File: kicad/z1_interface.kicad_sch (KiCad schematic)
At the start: 0 parts

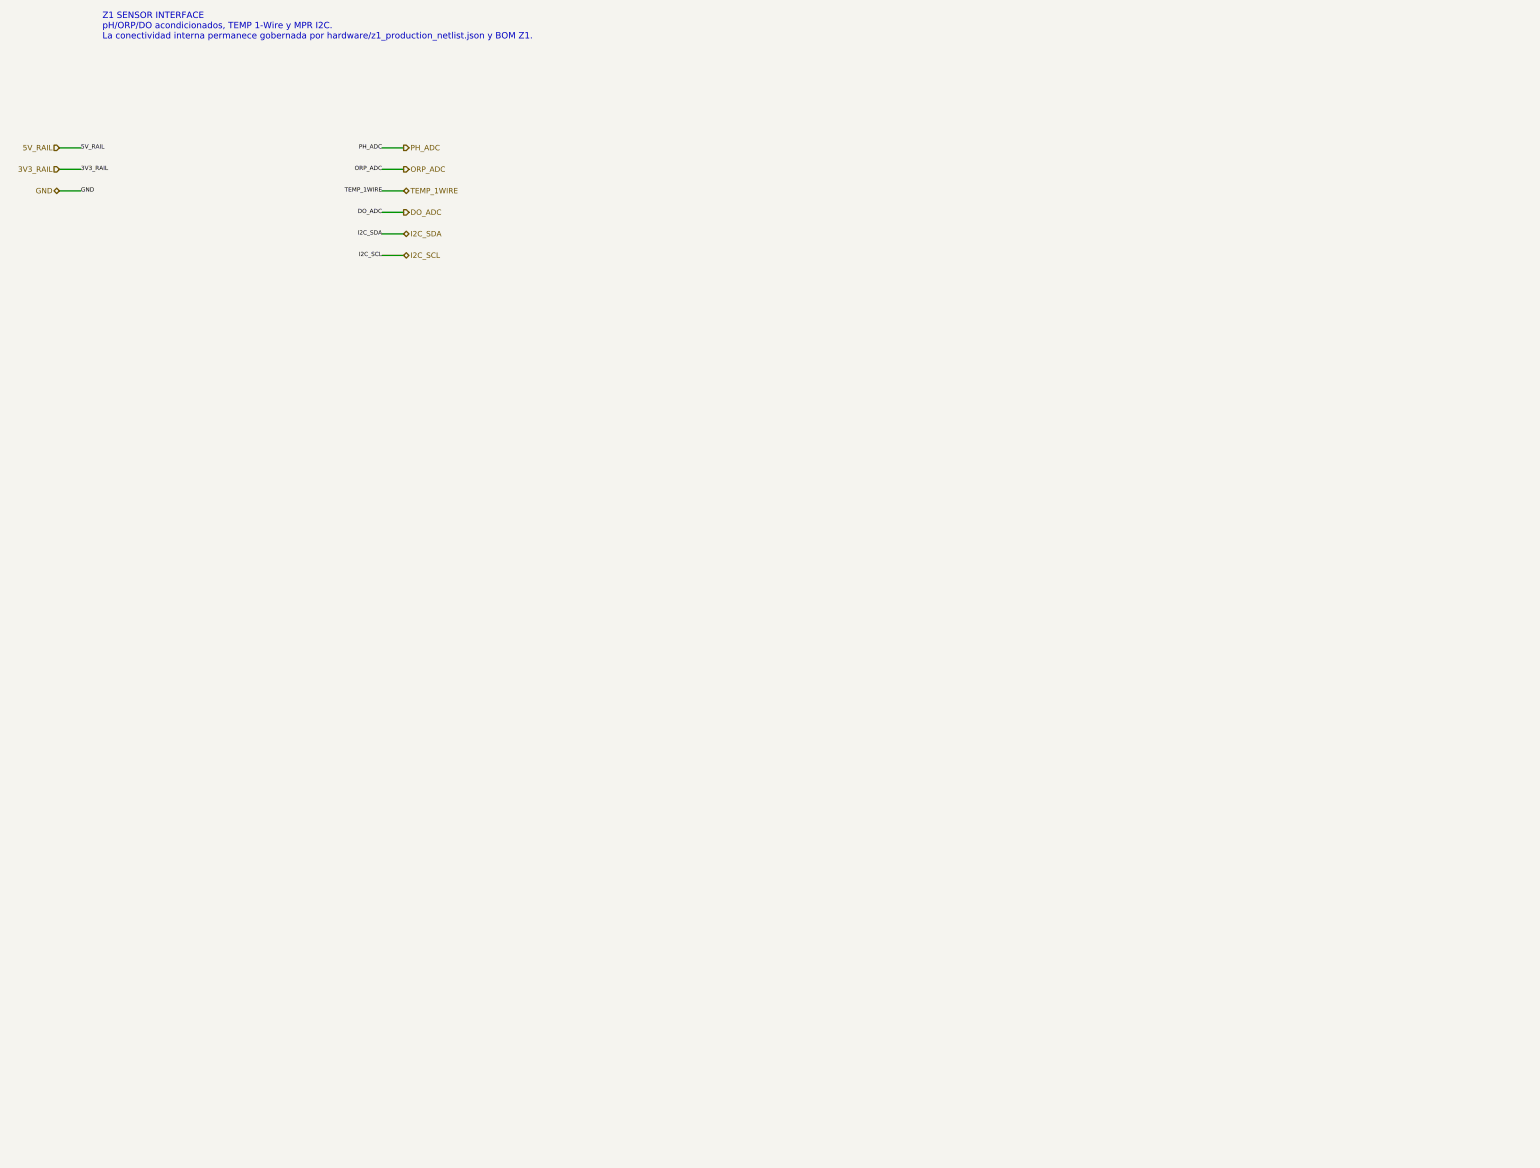
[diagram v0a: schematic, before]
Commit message: eda: materializar hierarchy de producción y cerrar ERC en cero (#15)
Materializa Z0–Z4 de forma determinista desde JSON/BOM, registra NFB_GEN, cierra seis links físicos verificados, elimina la deuda ERC de PR #14 y congela ERC=0/0 antes de placement. Mantiene placement, routing y geometría PCB fuera de alcance.
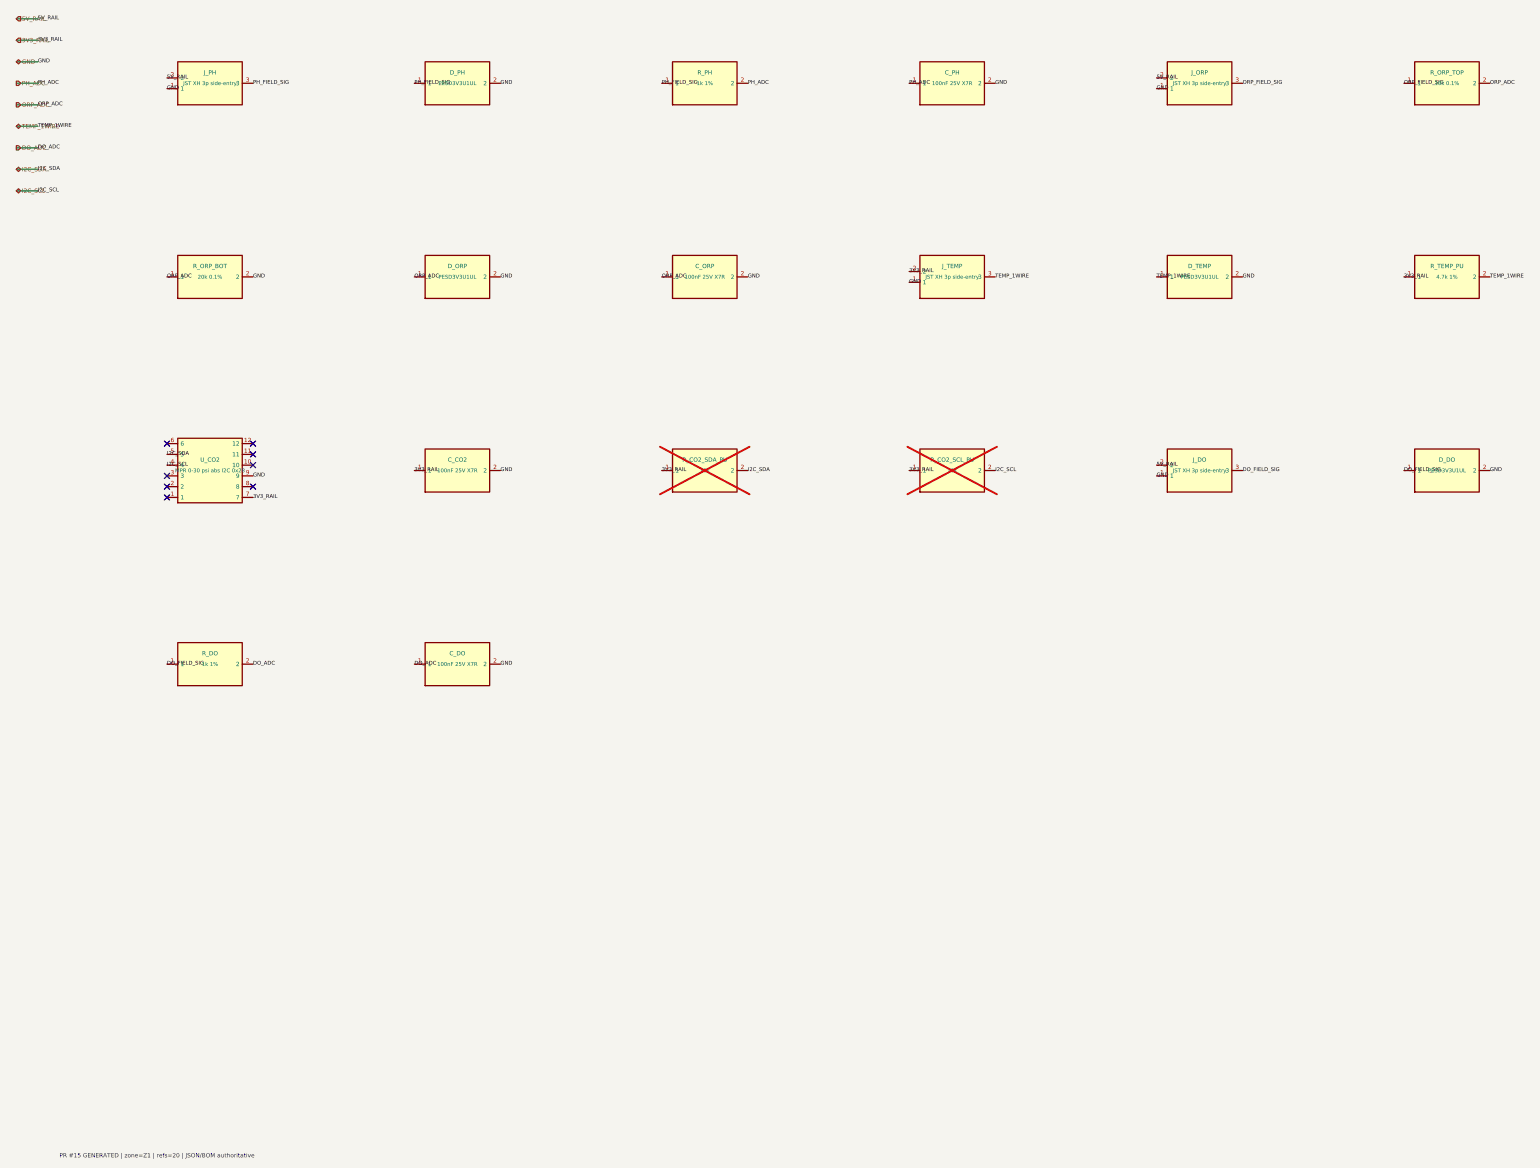
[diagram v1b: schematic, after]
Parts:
- added C_CO2: 100nF 25V X7R, Capacitor_SMD:C_0402_1005Metric, symbol NFB_GEN:SYM_C_CO2
- added C_DO: 100nF 25V X7R, Capacitor_SMD:C_0402_1005Metric, symbol NFB_GEN:SYM_C_DO
- added C_ORP: 100nF 25V X7R, Capacitor_SMD:C_0402_1005Metric, symbol NFB_GEN:SYM_C_ORP
- added C_PH: 100nF 25V X7R, Capacitor_SMD:C_0402_1005Metric, symbol NFB_GEN:SYM_C_PH
- added D_DO: PESD3V3U1UL, Diode_SMD:D_SOD-882, symbol NFB_GEN:SYM_D_DO
- added D_ORP: PESD3V3U1UL, Diode_SMD:D_SOD-882, symbol NFB_GEN:SYM_D_ORP
- added D_PH: PESD3V3U1UL, Diode_SMD:D_SOD-882, symbol NFB_GEN:SYM_D_PH
- added D_TEMP: PESD3V3U1UL, Diode_SMD:D_SOD-882, symbol NFB_GEN:SYM_D_TEMP
- added J_DO: JST XH 3p side-entry, Connector_JST:JST_XH_S3B-XH-A_1x03_P2.50mm_Horizontal, symbol NFB_GEN:SYM_J_DO
- added J_ORP: JST XH 3p side-entry, Connector_JST:JST_XH_S3B-XH-A_1x03_P2.50mm_Horizontal, symbol NFB_GEN:SYM_J_ORP
- added J_PH: JST XH 3p side-entry, Connector_JST:JST_XH_S3B-XH-A_1x03_P2.50mm_Horizontal, symbol NFB_GEN:SYM_J_PH
- added J_TEMP: JST XH 3p side-entry, Connector_JST:JST_XH_S3B-XH-A_1x03_P2.50mm_Horizontal, symbol NFB_GEN:SYM_J_TEMP
- added R_CO2_SCL_PU: 10k, Resistor_SMD:R_0402_1005Metric, symbol NFB_GEN:SYM_R_CO2_SCL_PU
- added R_CO2_SDA_PU: 10k, Resistor_SMD:R_0402_1005Metric, symbol NFB_GEN:SYM_R_CO2_SDA_PU
- added R_DO: 1k 1%, Resistor_SMD:R_0402_1005Metric, symbol NFB_GEN:SYM_R_DO
- added R_ORP_BOT: 20k 0.1%, Resistor_SMD:R_0402_1005Metric, symbol NFB_GEN:SYM_R_ORP_BOT
- added R_ORP_TOP: 10k 0.1%, Resistor_SMD:R_0402_1005Metric, symbol NFB_GEN:SYM_R_ORP_TOP
- added R_PH: 1k 1%, Resistor_SMD:R_0402_1005Metric, symbol NFB_GEN:SYM_R_PH
- added R_TEMP_PU: 4.7k 1%, Resistor_SMD:R_0402_1005Metric, symbol NFB_GEN:SYM_R_TEMP_PU
- added U_CO2: MPR 0-30 psi abs I2C 0x28, NFB:Honeywell_MPR_LongPort_12Pad, symbol NFB_GEN:SYM_U_CO2
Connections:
- net 3V3_RAIL: now also C_CO2.1, J_TEMP.2, R_CO2_SCL_PU.1, R_CO2_SDA_PU.1, R_TEMP_PU.1, U_CO2.7
- net 5V_RAIL: now also J_DO.2, J_ORP.2, J_PH.2
- net DO_ADC: now also C_DO.1, R_DO.2
- net GND: now also C_CO2.2, C_DO.2, C_ORP.2, C_PH.2, D_DO.2, D_ORP.2, D_PH.2, D_TEMP.2, J_DO.1, J_ORP.1, J_PH.1, J_TEMP.1, R_ORP_BOT.2, U_CO2.9
- net I2C_SCL: now also R_CO2_SCL_PU.2, U_CO2.4
- net I2C_SDA: now also R_CO2_SDA_PU.2, U_CO2.5
- net ORP_ADC: now also C_ORP.1, D_ORP.1, R_ORP_BOT.1, R_ORP_TOP.2
- net PH_ADC: now also C_PH.1, R_PH.2
- net TEMP_1WIRE: now also D_TEMP.1, J_TEMP.3, R_TEMP_PU.2
- new net DO_FIELD_SIG: D_DO.1, J_DO.3, R_DO.1
- new net ORP_FIELD_SIG: J_ORP.3, R_ORP_TOP.1
- new net PH_FIELD_SIG: D_PH.1, J_PH.3, R_PH.1
- no-connect marks 0 -> 8
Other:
- note added: "PR #15 GENERATED | zone=Z1 | refs=20 | JSON/BOM authoritative"
- note removed: "Z1 SENSOR INTERFACE pH/ORP/DO acondicionados, TEMP 1-Wire y MPR I2C. La conectividad interna permanece gobernada por hardware/z1_production_netlist.json y BOM Z1."
- title: NFB Insight PCBA v2 — Z1 Interface -> NFB Insight PCBA v2 — Z1 GENERATED PRODUCTION
